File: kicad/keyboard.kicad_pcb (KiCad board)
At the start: 2 copper layers, 84 parts, among them J1 USB_C_Receptacle_USB2.0_14P, J2 AudioJack4, J3 Conn_01x04_Pin, SW1 SW_Push, SW10 SW_Push, SW11 SW_Push, SW12 SW_Push, SW13 SW_Push, SW14 SW_Push, SW15 SW_Push, SW16 SW_Push, SW17 SW_Push, SW18 SW_Push, SW19 SW_Push, SW2 SW_Push, SW20 SW_Push, SW21 SW_Push, SW22 SW_Push, SW23 SW_Push, SW24 SW_Push, SW25 SW_Push, SW26 SW_Push, SW27 SW_Push, SW28 SW_Push, SW29 SW_Push, SW3 SW_Push, SW30 SW_Push, SW31 SW_Push, SW32 SW_Push, SW33 SW_Push, SW34 SW_Push, SW35 SW_Push, SW36 SW_Push, SW4 SW_Push, SW5 SW_Push, SW6 SW_Push, SW7 SW_Push, SW8 SW_Push, SW9 SW_Push, U1 AVR32DU32x-xPT

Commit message: replaced project name from kicad to keyboard and finished (I think) the pcb
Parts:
- C3, C4, C5, C6, C7: footprint Capacitor_THT:C_Axial_L3.8mm_D2.6mm_P7.50mm_Horizontal -> Capacitor_SMD:C_0603_1608Metric
- R2: renamed from C1; value C_Small -> R; footprint Capacitor_THT:C_Axial_L3.8mm_D2.6mm_P7.50mm_Horizontal -> Resistor_SMD:R_0603_1608Metric
- R3: renamed from C2; value C_Small -> R; footprint Capacitor_THT:C_Axial_L3.8mm_D2.6mm_P7.50mm_Horizontal -> Resistor_SMD:R_0603_1608Metric
- RV1: footprint Potentiometer_THT:Potentiometer_ACP_CA9-V10_Vertical_Hole -> Potentiometer_THT:Potentiometer_TT_P0915N
- SW1, SW2, SW3, SW34, SW4, SW5: footprint Button_Switch_Keyboard:SW_Cherry_MX_1.00u_PCB -> Button_Switch_Keyboard:SW_Cherry_MX_1.50u_PCB
- SW33: footprint Button_Switch_Keyboard:SW_Cherry_MX_1.00u_PCB -> Button_Switch_Keyboard:SW_Cherry_MX_1.25u_PCB
- SW35: footprint Button_Switch_Keyboard:SW_Cherry_MX_1.00u_PCB -> Button_Switch_Keyboard:SW_Cherry_MX_1.75u_PCB
- moved D5 196.7 mm to (67.2, 131.7), turned to -90 degrees
- moved D6 195.8 mm to (91.5, 53.0), turned to -90 degrees
- moved D7 193.5 mm to (91.8, 72.5), turned to -90 degrees
- moved D4 192.5 mm to (67.2, 112.2), turned to -90 degrees
- moved D1 192.1 mm to (67.2, 54.2), turned to -90 degrees
- moved D3 190.2 mm to (67.2, 92.8), turned to -90 degrees
- moved D2 190.2 mm to (67.2, 73.2), turned to -90 degrees
- moved D11 168.9 mm to (111.0, 43.8), turned to -90 degrees
- moved J3 168.5 mm to (82.5, 48.0), turned to 90 degrees
- moved D14 165.6 mm to (111.0, 103.2), turned to -90 degrees
- moved D12 164.9 mm to (111.0, 64.5), turned to -90 degrees
- moved D13 164.0 mm to (111.0, 84.0), turned to -90 degrees
- moved D10 161.4 mm to (91.5, 130.8), turned to -90 degrees
- moved D9 156.5 mm to (91.5, 111.8), turned to -90 degrees
- moved D8 154.1 mm to (91.5, 92.0), turned to -90 degrees
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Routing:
- net row5: track 0.00 -> 242.1 mm, vias 0 -> 2
- net row4: track 0.00 -> 219.5 mm, vias 0 -> 2
- net row3: track 0.00 -> 197.5 mm, vias 0 -> 2
- net col7: track 0.00 -> 193.3 mm, vias 0 -> 1
- net row2: track 0.00 -> 171.7 mm, vias 0 -> 2
- net col6: track 0.00 -> 170.8 mm, vias 0 -> 1
- net col5: track 0.00 -> 153.7 mm, vias 0 -> 1
- net scl: track 0.00 -> 144.0 mm, vias 0 -> 4
- net row1: track 0.00 -> 140.9 mm
- net sda: track 0.00 -> 136.6 mm, vias 0 -> 4
- net col4: track 0.00 -> 126.5 mm, vias 0 -> 1
- net Net-(U1-PC3): track 0.00 -> 113.6 mm, vias 0 -> 1
- net col3: track 0.00 -> 110.5 mm, vias 0 -> 1
- net col1: track 0.00 -> 101.7 mm, vias 0 -> 1
- net col2: track 0.00 -> 88.0 mm, vias 0 -> 1
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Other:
- board outline added: 163 x 121 mm
- board text added: "A N D E R S"

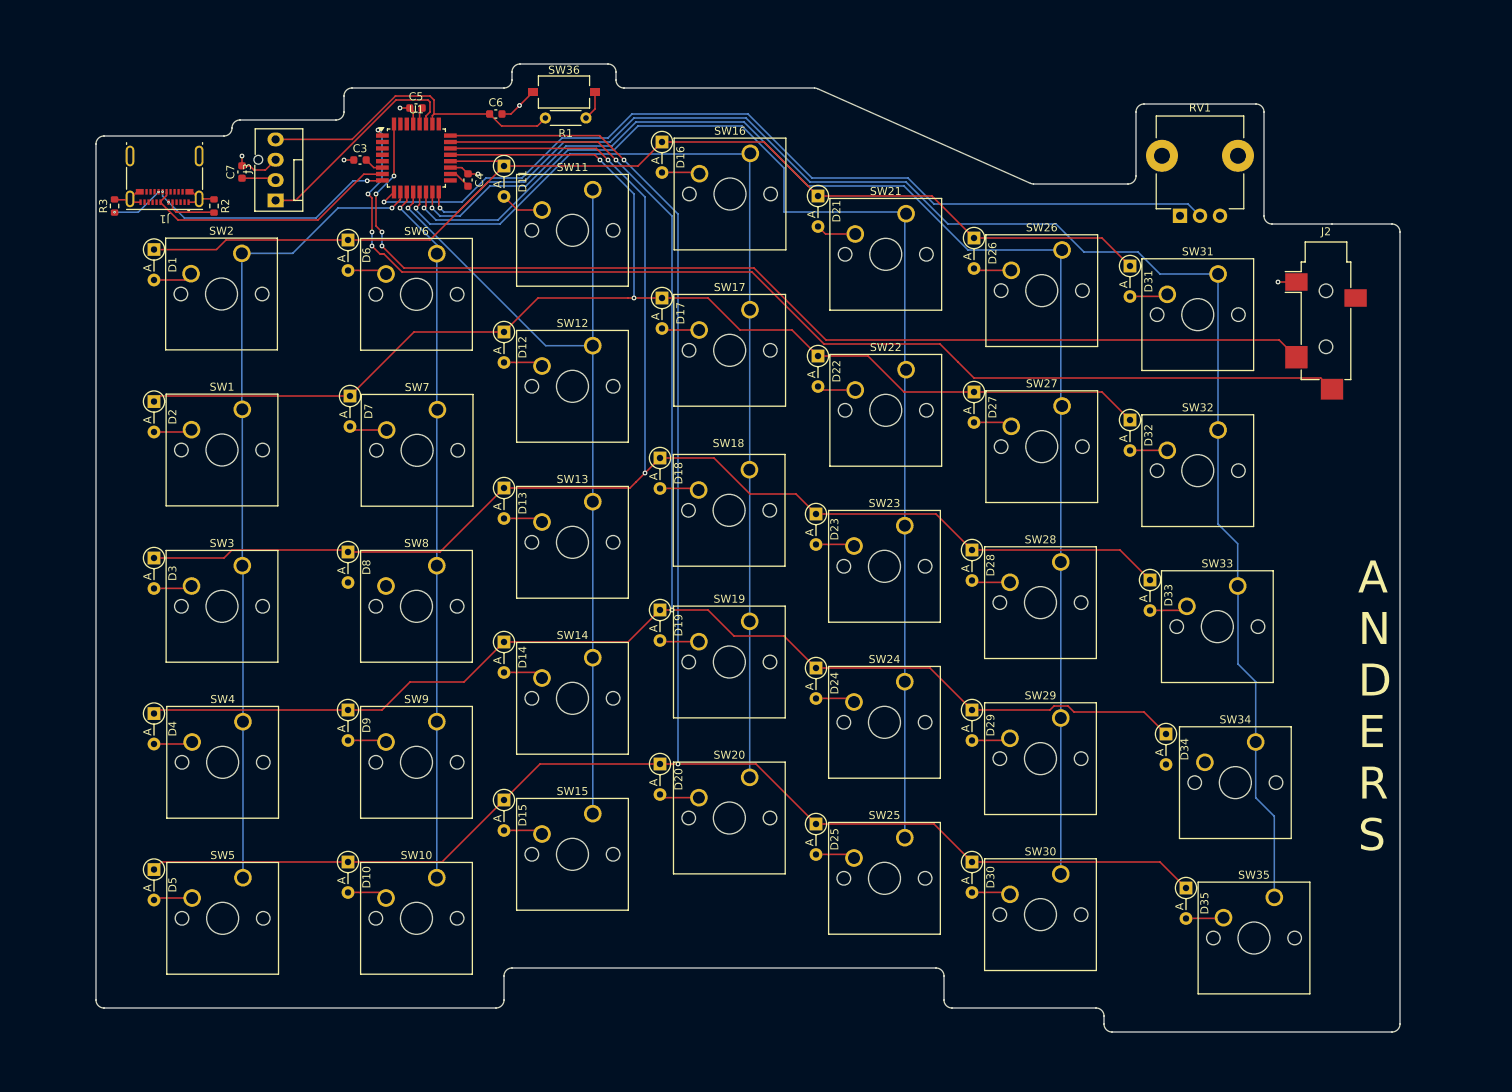
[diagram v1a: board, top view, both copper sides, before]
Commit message: finished up left-side pcb, not sure if right should go in the same project or to make a new one, plotted gerber files
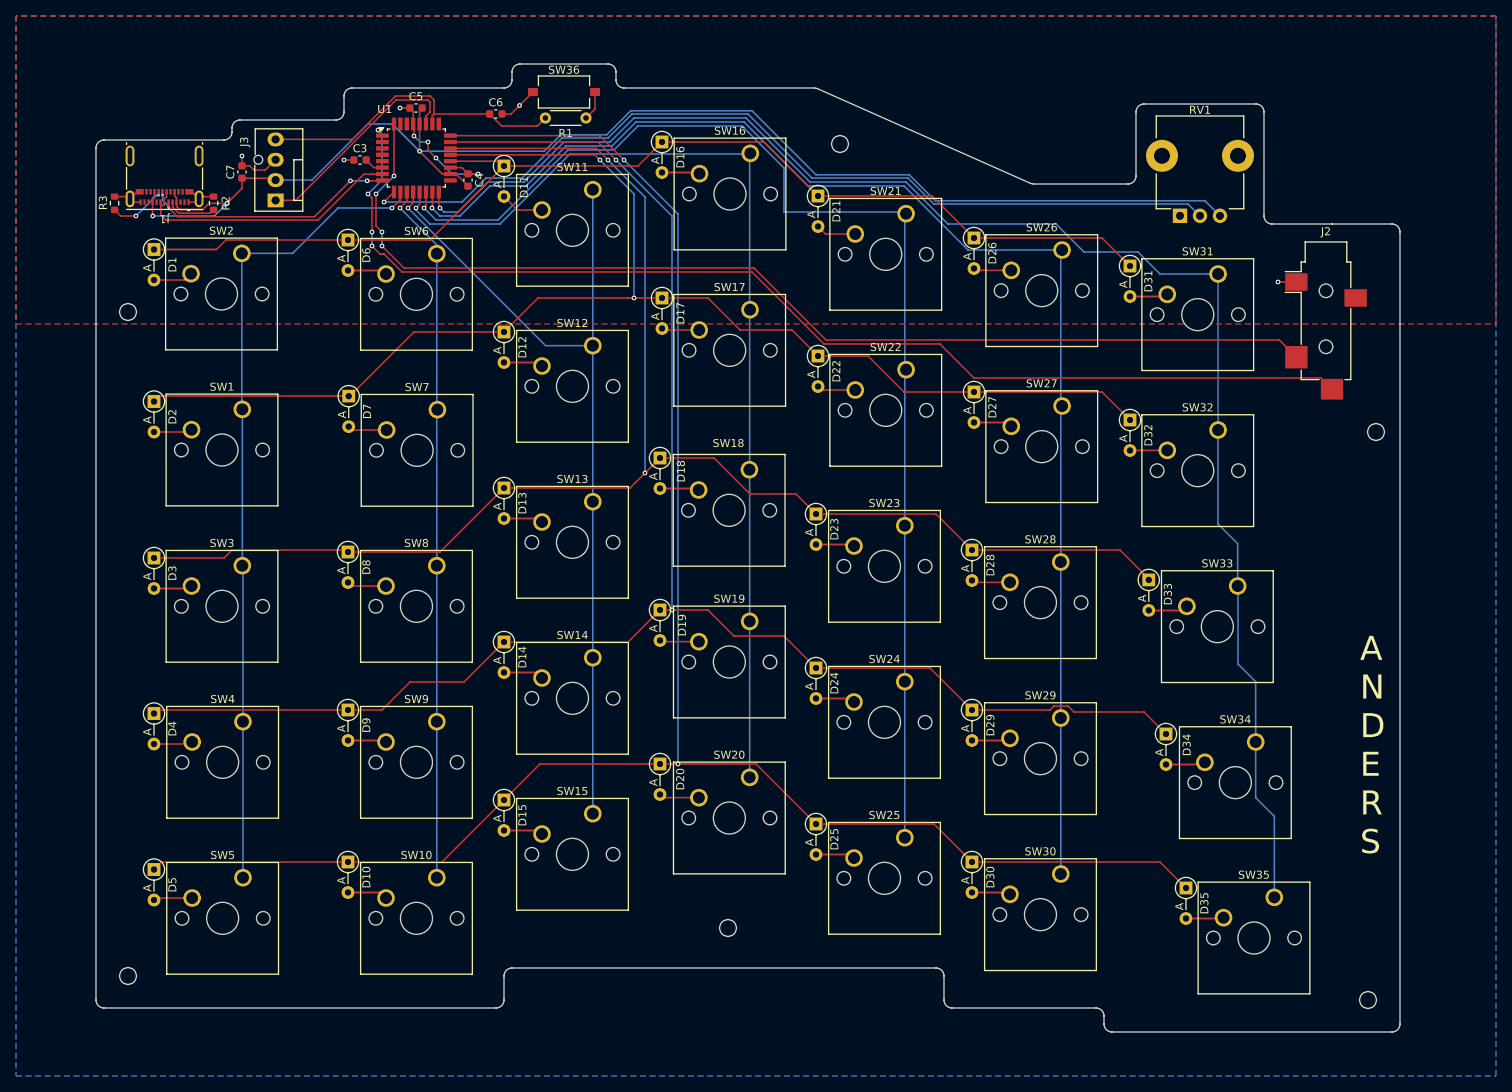
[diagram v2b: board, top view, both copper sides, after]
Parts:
- added REF**: MountingHole_2.1mm, MountingHole:MountingHole_2.1mm, F.Cu at (220.0, 77.0)
- added REF**: MountingHole_2.1mm, MountingHole:MountingHole_2.1mm, F.Cu at (139.0, 139.0)
- added REF**: MountingHole_2.1mm, MountingHole:MountingHole_2.1mm, F.Cu at (153.0, 41.0)
- added REF**: MountingHole_2.1mm, MountingHole:MountingHole_2.1mm, F.Cu at (64.0, 62.0)
- added REF**: MountingHole_2.1mm, MountingHole:MountingHole_2.1mm, F.Cu at (219.0, 148.0)
- added REF**: MountingHole_2.1mm, MountingHole:MountingHole_2.1mm, F.Cu at (64.0, 145.0)
- moved R2 0.35 mm to (74.7, 48.4), turned to 90 degrees
- moved R3 0.35 mm to (62.3, 48.4), turned to 90 degrees
- moved D7 0.16 mm to (91.6, 72.5)
- moved D33 0.15 mm to (191.6, 95.5)
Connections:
- R2 pad 1: GND -> Net-(J1-CC1)
- R2 pad 2: Net-(J1-CC1) -> GND
- R3 pad 1: GND -> Net-(J1-CC2)
- R3 pad 2: Net-(J1-CC2) -> GND
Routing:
- net VDD: track 9.28 -> 173.4 mm, vias 0 -> 3
- net GND: track 32.0 -> 44.4 mm, vias 6 -> 9
- net Net-(D34-A): track 0.00 -> 4.97 mm
- net Net-(D8-A): track 0.00 -> 4.93 mm
- net dm: track 32.7 -> 34.2 mm
- net Net-(J1-CC2): track 6.57 -> 7.53 mm
- net dp: track 31.1 -> 32.1 mm, vias 3 -> 4
- added copper zone on B.Cu, net GND
- added copper zone on F.Cu, net VDD
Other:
- outline, holes or cut-outs redrawn

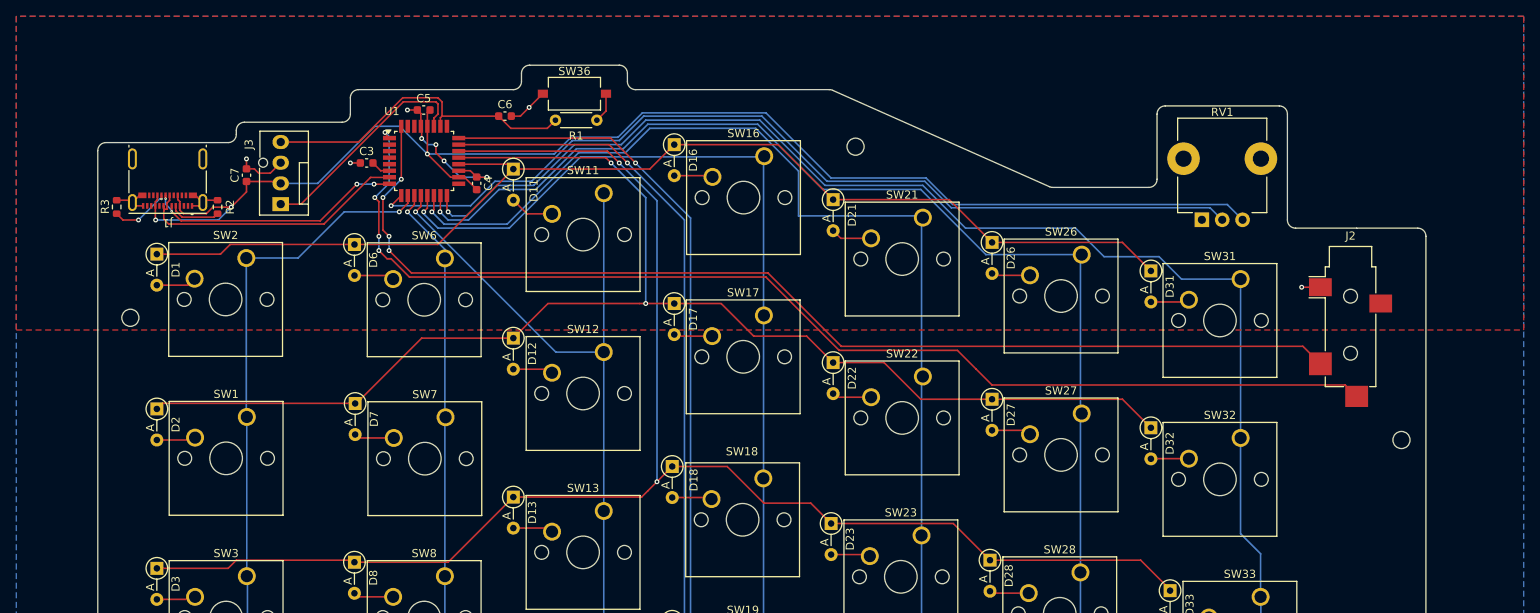
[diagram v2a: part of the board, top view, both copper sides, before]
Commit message: changed usb receptacle footprint
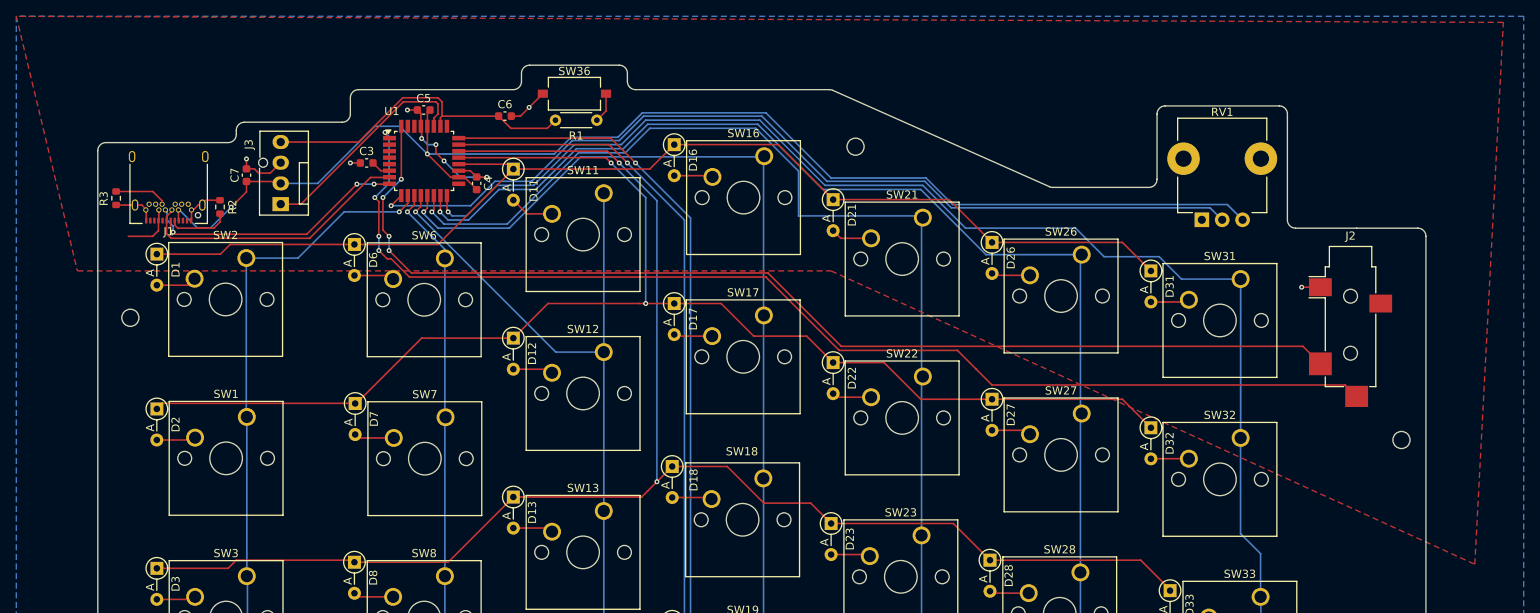
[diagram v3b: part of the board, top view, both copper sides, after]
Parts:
- J1: footprint Connector_USB:USB_C_Receptacle_Molex_105450-0101 -> Connector_USB:USB_C_Receptacle_Amphenol_12401548E4-2A
- moved R3 1.08 mm to (62.2, 47.3), turned to -90 degrees
- moved R2 0.30 mm to (75.0, 48.4)
- moved J1 0.13 mm to (68.7, 45.1)
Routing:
- net VDD: track 173.4 -> 167.9 mm, vias 3 -> 2
- net dp: track 32.1 -> 33.9 mm, vias 4 -> 3
- net Net-(J1-CC1): track 6.26 -> 7.60 mm
- net Net-(J1-CC2): track 7.53 -> 6.54 mm, vias 2 -> 0
